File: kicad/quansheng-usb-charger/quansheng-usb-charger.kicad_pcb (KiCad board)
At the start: 2 copper layers, 42.8 x 48 mm, 32 parts, among them J1 USB_C_Receptacle_USB2.0, U1 IP2326

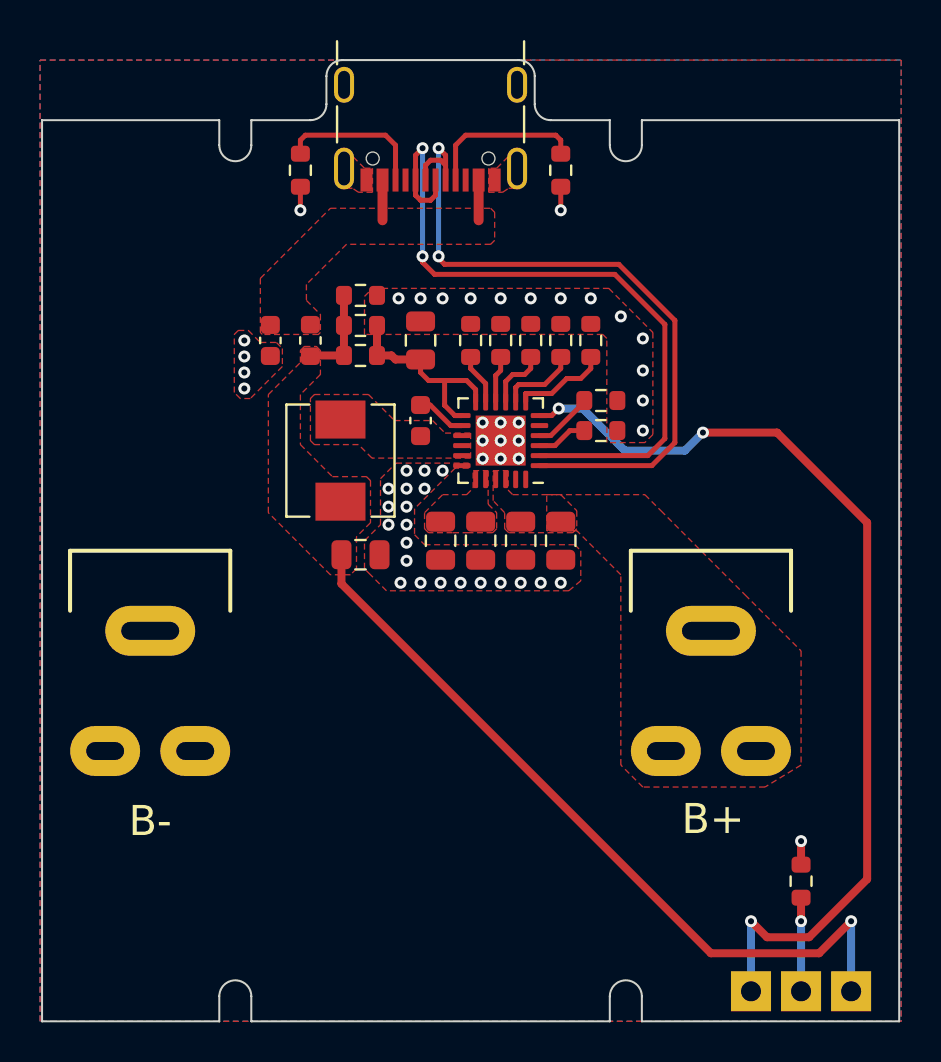
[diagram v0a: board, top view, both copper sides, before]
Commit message: Add Tooling Holes
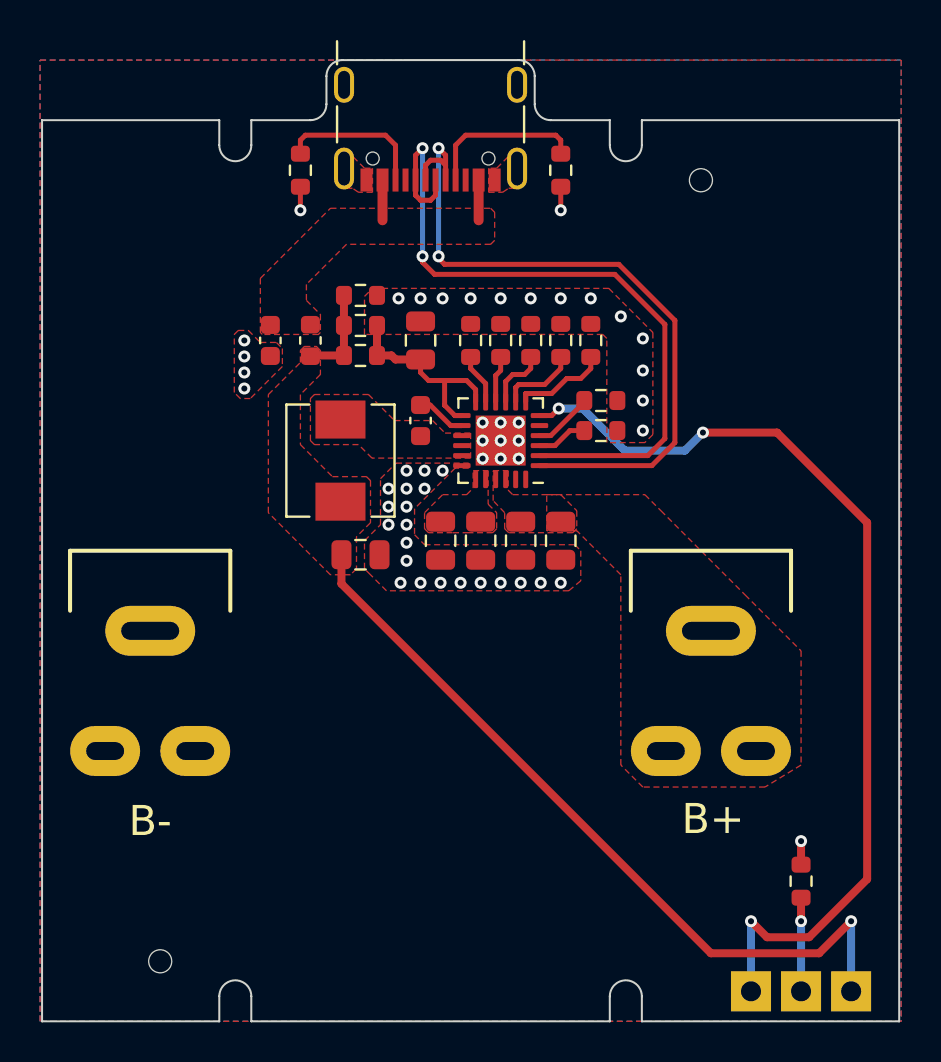
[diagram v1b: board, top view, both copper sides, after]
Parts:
- added H1: ToolingHole, Project:TOOLING-HOLE, F.Cu at (133.0, 88.0)
- added H2: ToolingHole, Project:TOOLING-HOLE, F.Cu at (106.0, 127.0)
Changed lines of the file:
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@@
     )
+  )
+  (footprint "Project:TOOLING-HOLE" (layer "F.Cu")
+    (at 133 88)
+    (property "Sheetfile" "quansheng-usb-charger.kicad_sch")
+    (property "Sheetname" "")
+    (attr through_hole exclude_from_pos_files exclude_from_bom)
+    (fp_text reference "H1" (at -0.508 -2.54 unlocked) (layer "F.SilkS") hide
+      (effects (font (size 1 1) (thickness 0.15)))
+    )
+    (fp_text value "ToolingHole" (at 0 3.048 unlocked) (layer "F.Fab") hide
+      (effects (font (size 1 1) (thickness 0.15)))
+    )
+    (fp_text user "${REFERENCE}" (at 0 4.572 unlocked) (layer "F.Fab") hide
+      (effects (font (size 1 1) (thickness 0.15)))
+    )
+    (pad "" np_thru_hole circle (at 0 0) (size 1.152 1.152) (drill 1.152) (layers F&B.Cu *.Mask)
+      (solder_mask_margin 0.15) (clearance 0.25))
+  )
+  (footprint "Project:TOOLING-HOLE" (layer "F.Cu")
+    (at 106 127)
+    (property "Sheetfile" "quansheng-usb-charger.kicad_sch")
+    (property "Sheetname" "")
+    (attr through_hole exclude_from_pos_files exclude_from_bom)
+    (fp_text reference "H2" (at -0.508 -2.54 unlocked) (layer "F.SilkS") hide
+      (effects (font (size 1 1) (thickness 0.15)))
+    )
+    (fp_text value "ToolingHole" (at 0 3.048 unlocked) (layer "F.Fab") hide
+      (effects (font (size 1 1) (thickness 0.15)))
+    )
+    (fp_text user "${REFERENCE}" (at 0 4.572 unlocked) (layer "F.Fab") hide
+      (effects (font (size 1 1) (thickness 0.15)))
+    )
+    (pad "" np_thru_hole circle (at 0 0) (size 1.152 1.152) (drill 1.152) (layers F&B.Cu *.Mask)
+      (solder_mask_margin 0.15) (clearance 0.25))
   )
   (footprint "Resistor_SMD:R_0603_1608Metric" (layer "F.Cu")

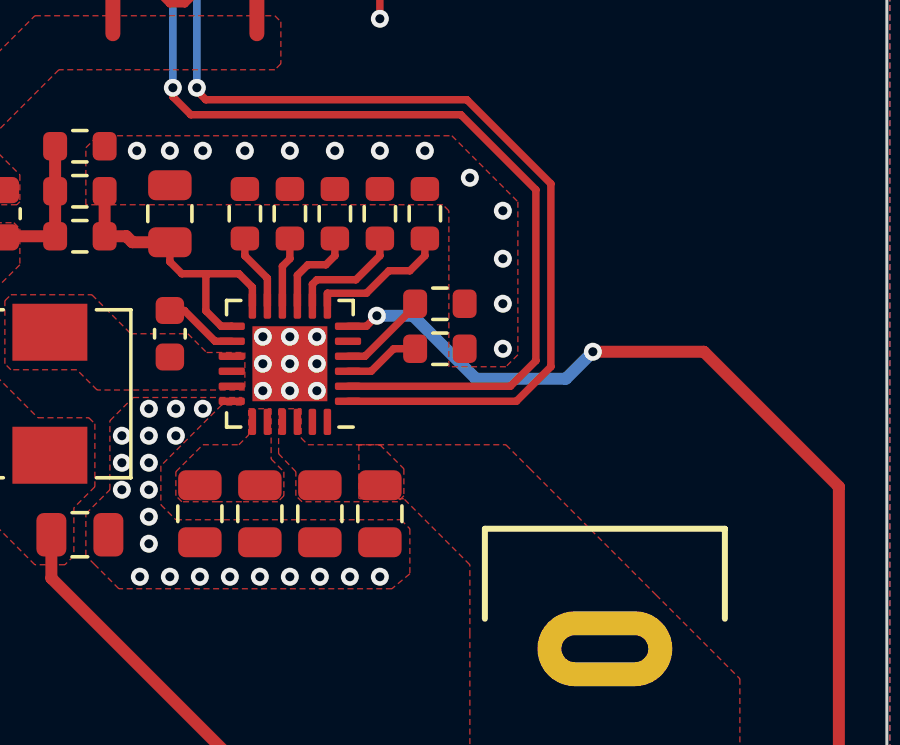
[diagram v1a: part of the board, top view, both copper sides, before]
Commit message: Don't use the built-in USB AFC standard
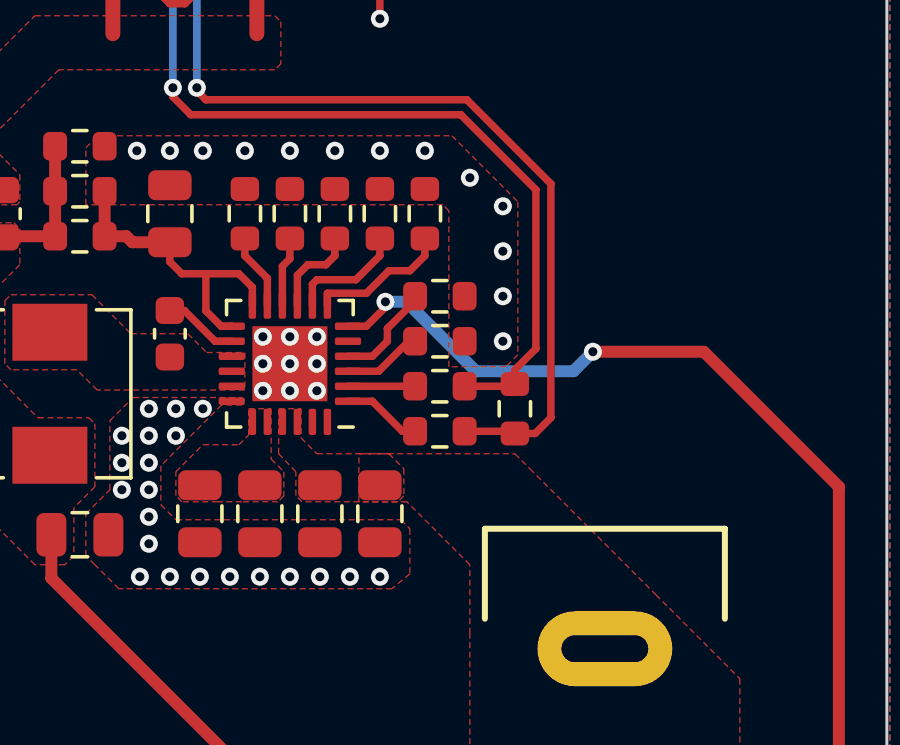
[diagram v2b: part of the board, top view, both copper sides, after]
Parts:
- added R14: 1R, Resistor_SMD:R_0603_1608Metric, F.Cu at (130.5, 102.5)
- added R15: NC, Resistor_SMD:R_0603_1608Metric, F.Cu at (128.0, 103.2)
- added R16: NC, Resistor_SMD:R_0603_1608Metric, F.Cu at (128.0, 101.8)
- R9: value 120K -> NC
- moved R11 0.25 mm to (128.0, 98.8)
- moved R4 0.25 mm to (128.0, 100.2)
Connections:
- U1 pad 1: Net-(J1-PadA7) -> Net-(U1-Pad1)
- U1 pad 2: Net-(J1-PadA6) -> Net-(U1-Pad2)
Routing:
- net Net-(J1-PadA6): track 35.9 -> 32.0 mm
- net Net-(U1-Pad1): track 0.00 -> 2.65 mm
- net Net-(J1-PadA7): track 35.6 -> 33.2 mm
- net Net-(U1-Pad2): track 0.00 -> 2.24 mm
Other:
- board text added: "Quansheng USB Charger Mod V1.1, Simon K."
- board text removed: "Quansheng USB Charger Mod V1.0, Simon K."

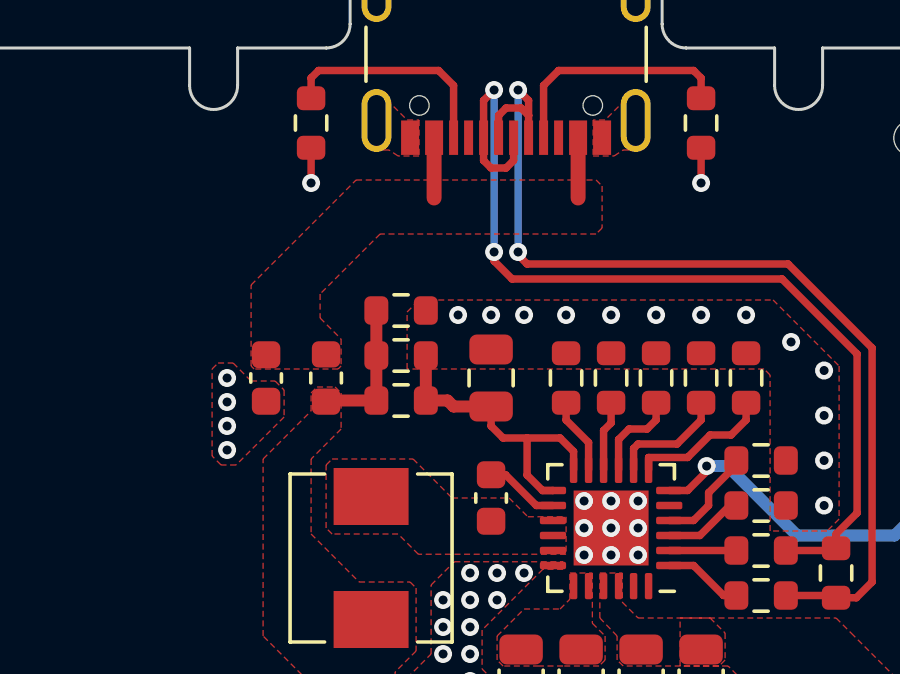
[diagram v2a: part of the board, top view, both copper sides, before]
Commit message: Add jumper pad for optional 1.5A charging current
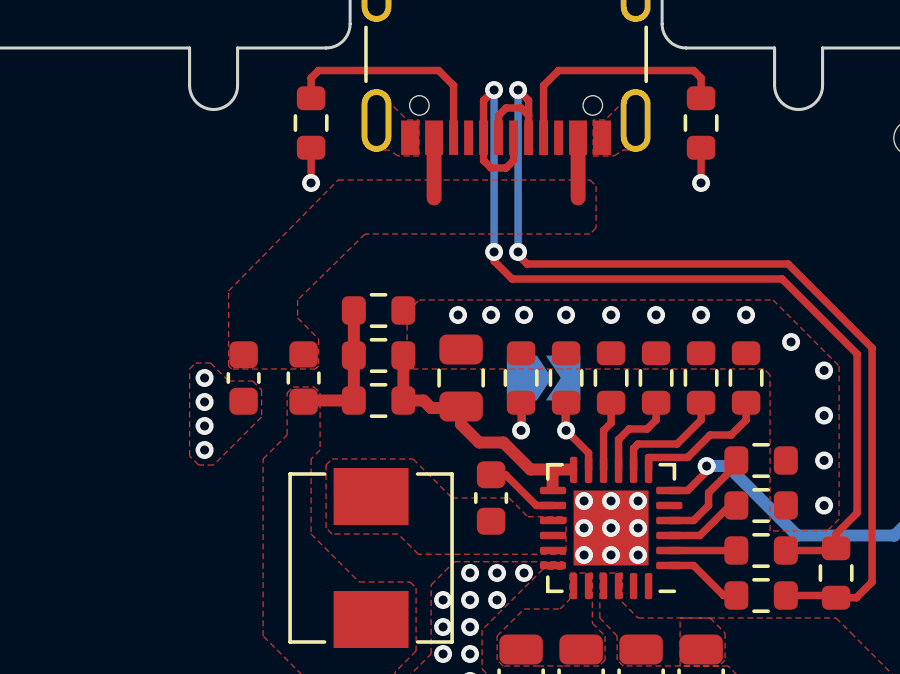
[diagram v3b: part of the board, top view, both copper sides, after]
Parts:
- added JP1: ISET, Jumper:SolderJumper-2_P1.3mm_Open_TrianglePad1.0x1.5mm, B.Cu at (120.8, 96.0)
- added R17: 120K, Resistor_SMD:R_0603_1608Metric, F.Cu at (121.5, 96.0)
- moved R12 1.50 mm to (120.0, 96.0)
- moved C2 1.00 mm to (118.0, 96.0)
- moved C1 0.75 mm to (110.8, 96.0)
- moved FB1 0.75 mm to (112.8, 96.0)
- moved R13 0.75 mm to (115.2, 95.2)
- moved R3 0.75 mm to (115.2, 93.8)
- moved R6 0.75 mm to (115.2, 96.8)
- moved REF** 0.25 mm to (103.8, 93.5)
- moved REF** 0.25 mm to (119.2, 118.5)
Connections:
- U1 pad 11: Net-(R12-Pad2) -> Net-(U1-Pad11)
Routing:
- net Net-(U1-Pad11): track 0.00 -> 4.31 mm, vias 0 -> 1
- net Net-(C2-Pad1): track 10.4 -> 9.16 mm
- net Net-(R12-Pad2): track 2.55 -> 2.69 mm, vias 0 -> 1
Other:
- board text added: "CLOSED 1.5A"
- board text added: "OPEN 0.75A"
